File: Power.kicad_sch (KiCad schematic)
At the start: 28 parts, among them Q1 AO3401A, U1 AMS1117-5.0, U2 AMS1117-3.3, U3 NE5532, X1 PEDAL_COMBO_TOP

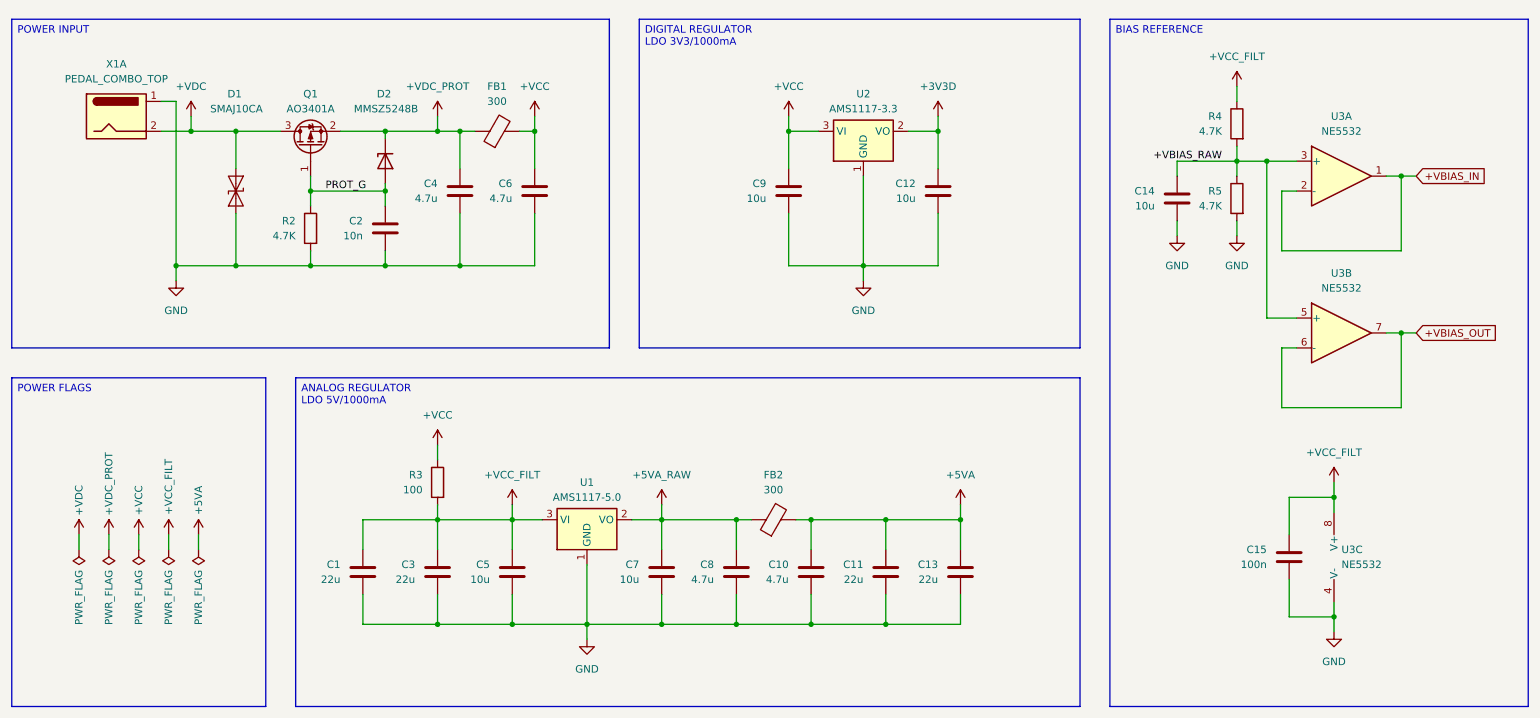
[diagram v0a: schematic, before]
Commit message: Buffer and layout
Updated the input and output buffers.
Updated the board layout.
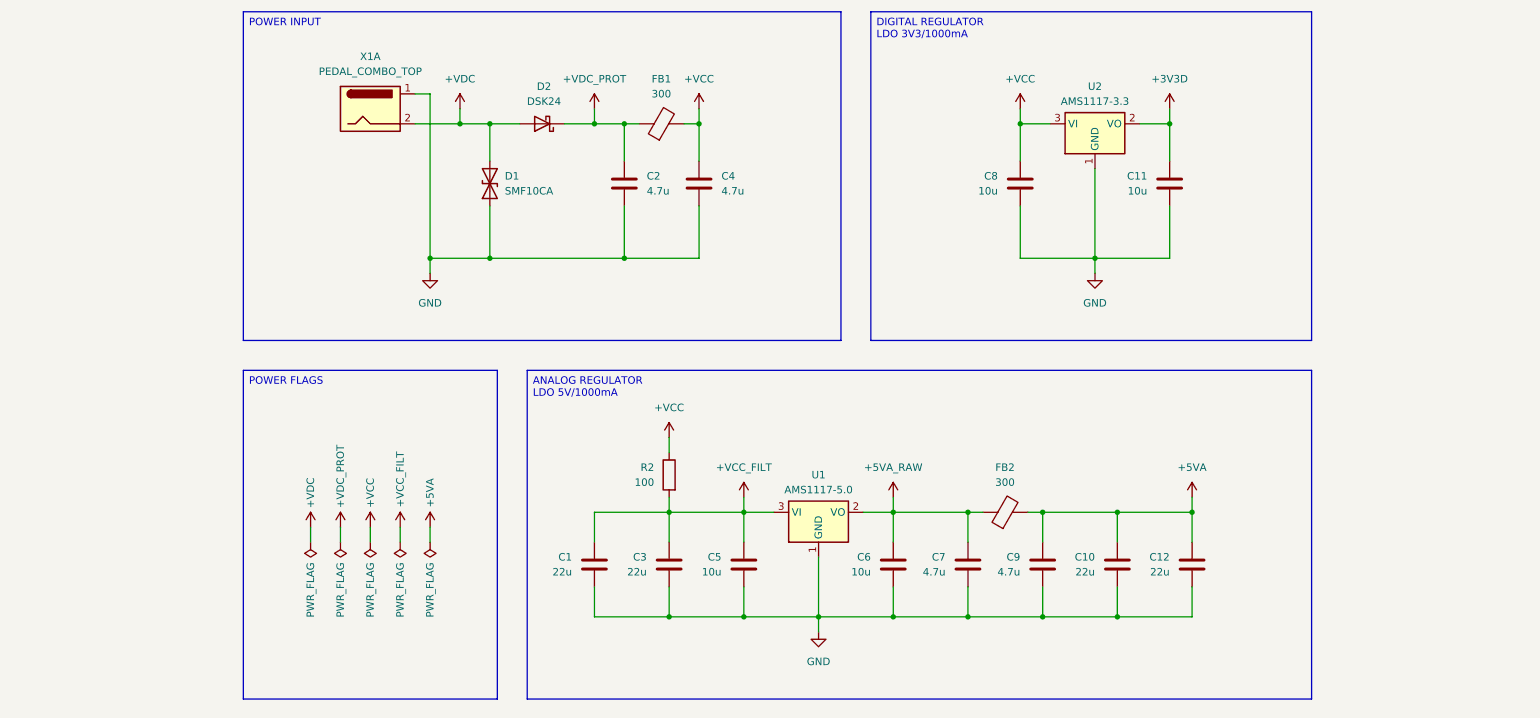
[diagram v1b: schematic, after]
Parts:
- removed C14: 10u, Capacitor_SMD:C_1206_3216Metric, symbol Device:C
- removed C15: 100n, Capacitor_SMD:C_0603_1608Metric, symbol Device:C
- removed C2: 10n, Capacitor_SMD:C_0603_1608Metric, symbol Device:C
- removed D1: SMAJ10CA, Diode_SMD:D_SMA, symbol Diode:SMAJ10CA
- removed D2: MMSZ5248B, Diode_SMD:D_SOD-123, symbol Device:D_Zener
- removed Q1: AO3401A, Package_TO_SOT_SMD:SOT-23, symbol Transistor_FET:AO3401A
- removed R2, R4, R5: 4.7K, Resistor_SMD:R_0603_1608Metric, symbol Device:R
- removed U3: NE5532, Package_SO:SOIC-8_3.9x4.9mm_P1.27mm, symbol Amplifier_Operational:NE5532
- added D1: SMF10CA, Diode_SMD:D_SOD-123F, symbol Device:D_TVS
- added D2: DSK24, Diode_SMD:D_SOD-123F, symbol Device:D_Schottky
- renumbered C11 to C10, C12 to C11, C13 to C12, C4 to C2, C6 to C4, C7 to C6, C8 to C7, C9 to C8, C10 to C9, R3 to R2
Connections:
- net +VDC: now also D1.2 (A2), D2.2 (A)
- net +VDC_PROT: now also D2.1 (K)
- net GND: now also D1.1 (A1)
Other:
- moved on the sheet: C1, C10, C11, C12, C2, C3, C4, C5, C6, C7, C8, C9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
